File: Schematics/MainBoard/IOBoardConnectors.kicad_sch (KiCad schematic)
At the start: 8 parts, among them J2 SubModule 1, J3 SubModule 1, J4 SubModule 1, J5 SubModule 1, J6 SubModule 1, J7 SubModule 1, J8 SubModule 1, J9 SubModule 1

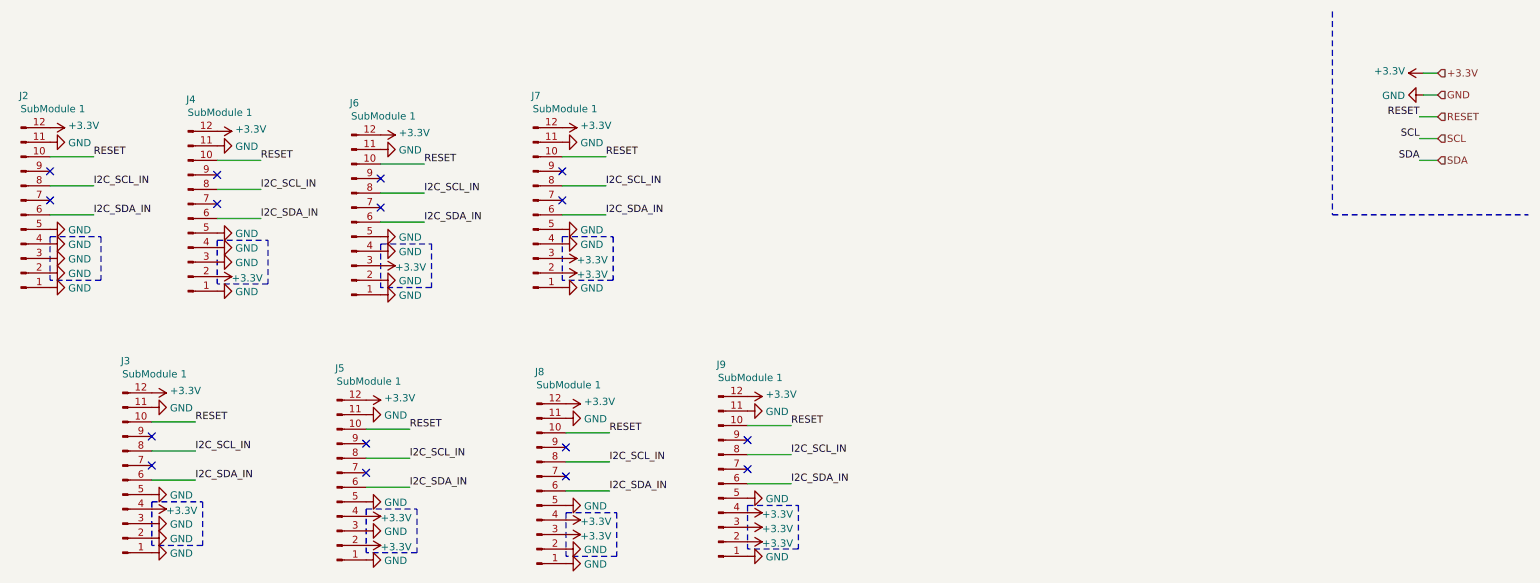
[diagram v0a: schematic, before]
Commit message: Finished circuit - pre mousebites
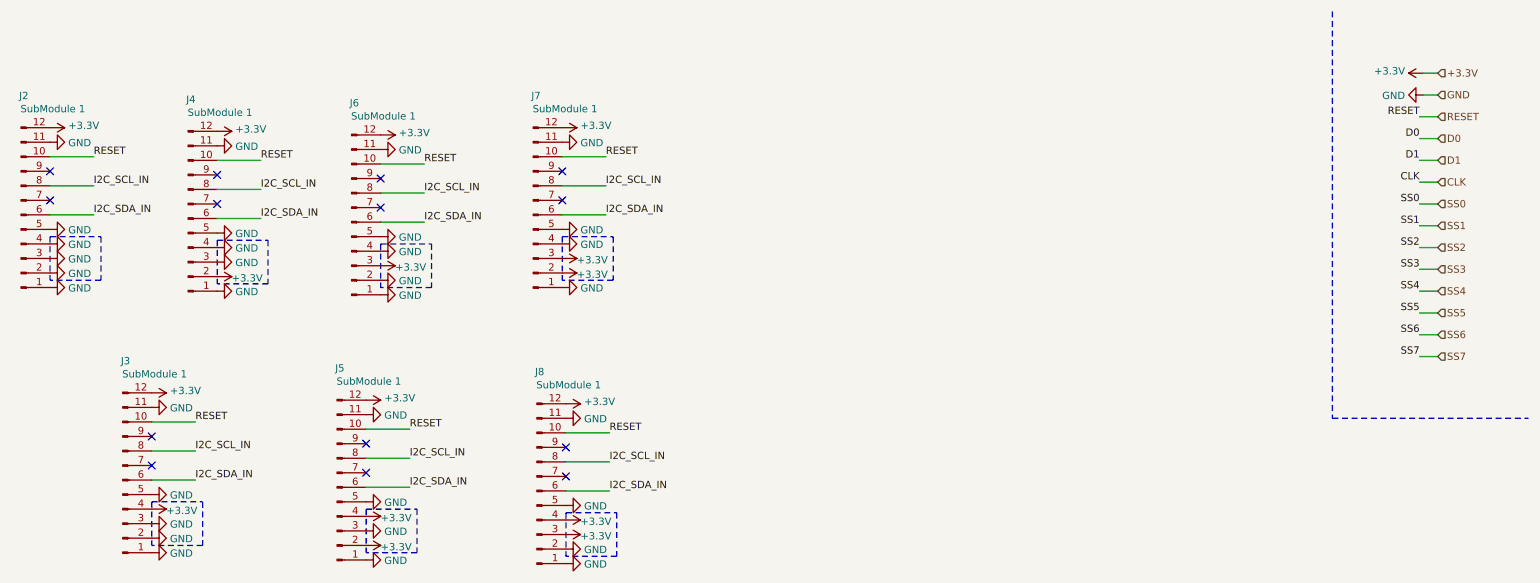
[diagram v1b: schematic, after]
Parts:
- removed J9: SubModule 1, Connector_PinHeader_2.54mm:PinHeader_2x06_P2.54mm_Vertical_SMD, symbol Connector:Conn_01x12_Male
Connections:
- no-connect marks 16 -> 14
